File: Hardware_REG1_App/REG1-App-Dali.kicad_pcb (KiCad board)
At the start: 2 copper layers, 83 x 32.8 mm, 27 parts, among them J1 REG1_App_Connector, J2 Dali, Q1 BSS123, Q2 BC857, U1 EL817S1(C)(TU)-F, U2 EL817S1(C)(TU)-F, U3 STN93003, U4 STN1HNK60

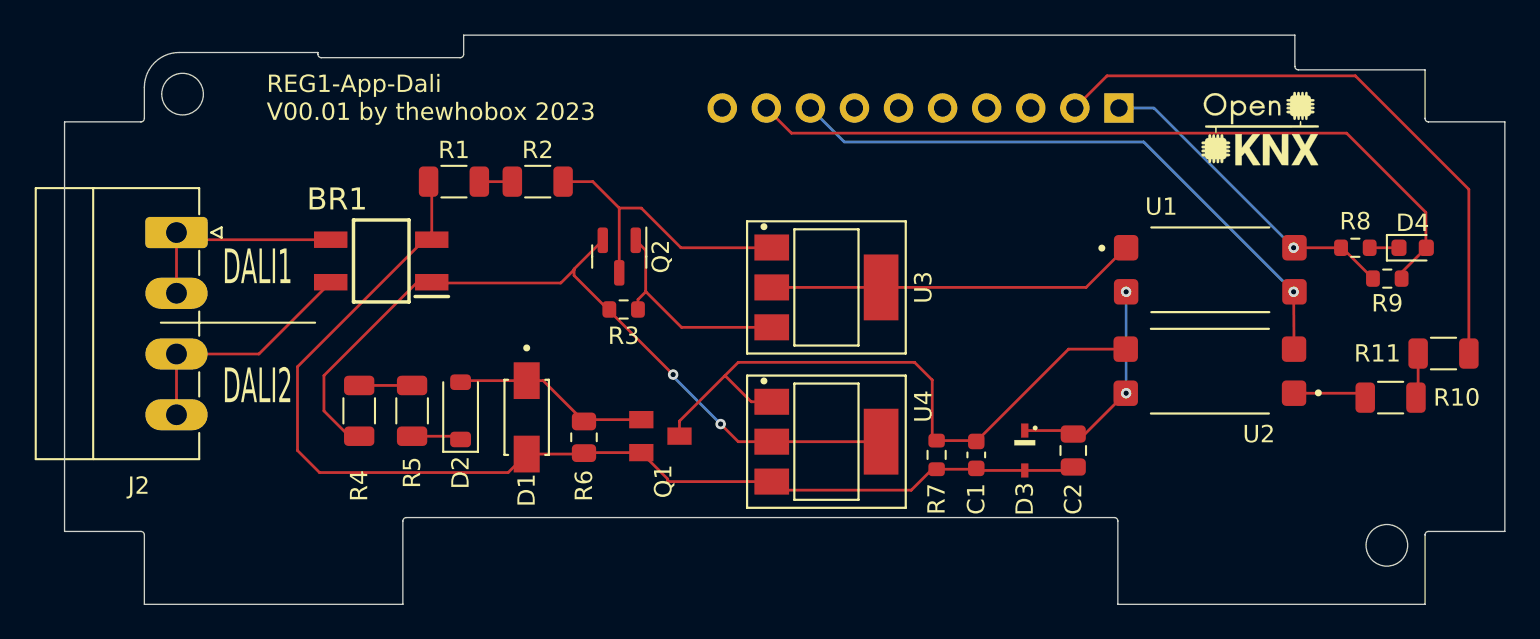
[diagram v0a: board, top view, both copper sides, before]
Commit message: adapted to REG1-V1 and JLCPCB fabrication toolkit
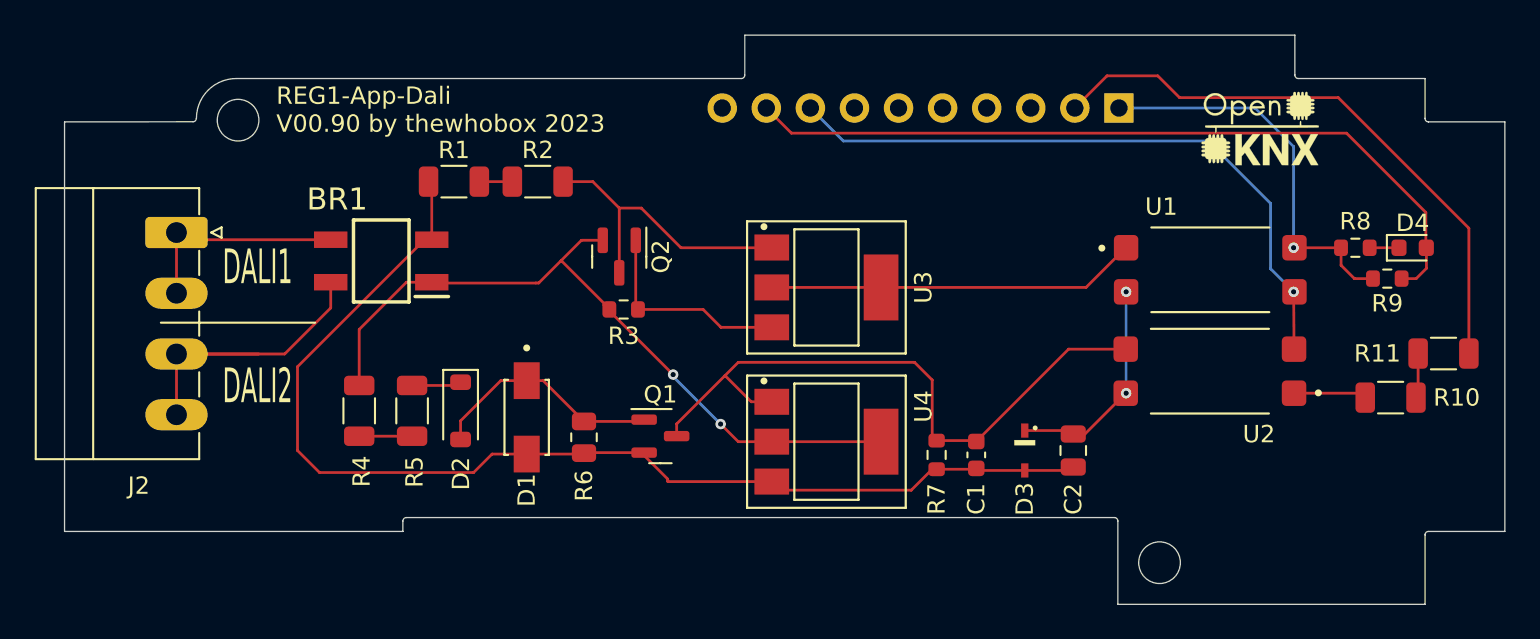
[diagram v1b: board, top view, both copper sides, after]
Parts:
- Q1: footprint DALI:SOT23 -> Package_TO_SOT_SMD:SOT-23
- turned D2 to -90 degrees
- turned Q1 to 0 degrees
- turned R4 to 90 degrees
- turned R5 to -90 degrees
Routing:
- net Net-(BR1-~_2): track 13.5 -> 19.1 mm
- net /D_RX: track 18.7 -> 22.7 mm
- net Net-(D2-A): track 11.5 -> 14.0 mm
- net GND: track 35.6 -> 37.8 mm
- net Dali+: track 45.5 -> 43.6 mm
- net /D_TX: track 35.6 -> 34.3 mm
- net +3.3V: track 44.9 -> 45.8 mm
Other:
- outline, holes or cut-outs redrawn
- board text added: "REG1-App-Dali V00.90 by thewhobox 2023"
- board text removed: "REG1-App-Dali V00.01 by thewhobox 2023"
